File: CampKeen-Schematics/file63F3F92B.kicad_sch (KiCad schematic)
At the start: 36 parts, among them Q42 2N7000, Q43 2N7000, Q44 IRF9Z34NPBF, Q45 IRF9Z34NPBF, Q46 2N7000, Q47 IRF9Z34NPBF, Q48 2N7000, Q49 IRF9Z34NPBF, Q50 2N7000, Q51 IRF9Z34NPBF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

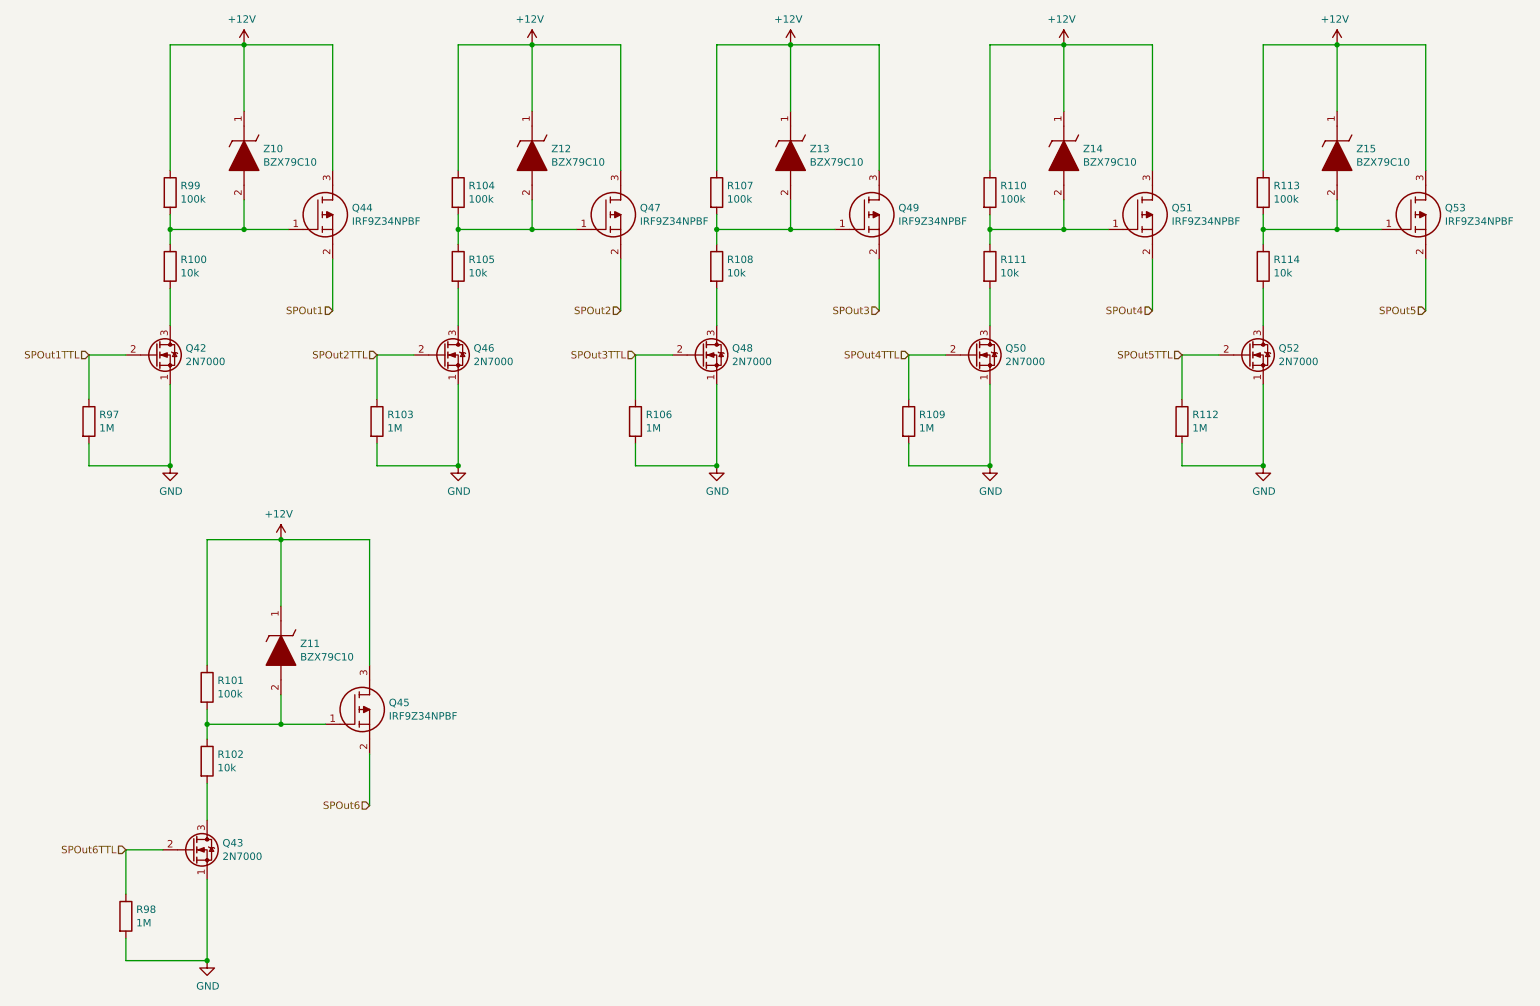
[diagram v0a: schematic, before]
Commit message: alright massive changes. some part switches and some reassignments. mostly it's switching out stuff for SMD so that i have more space.
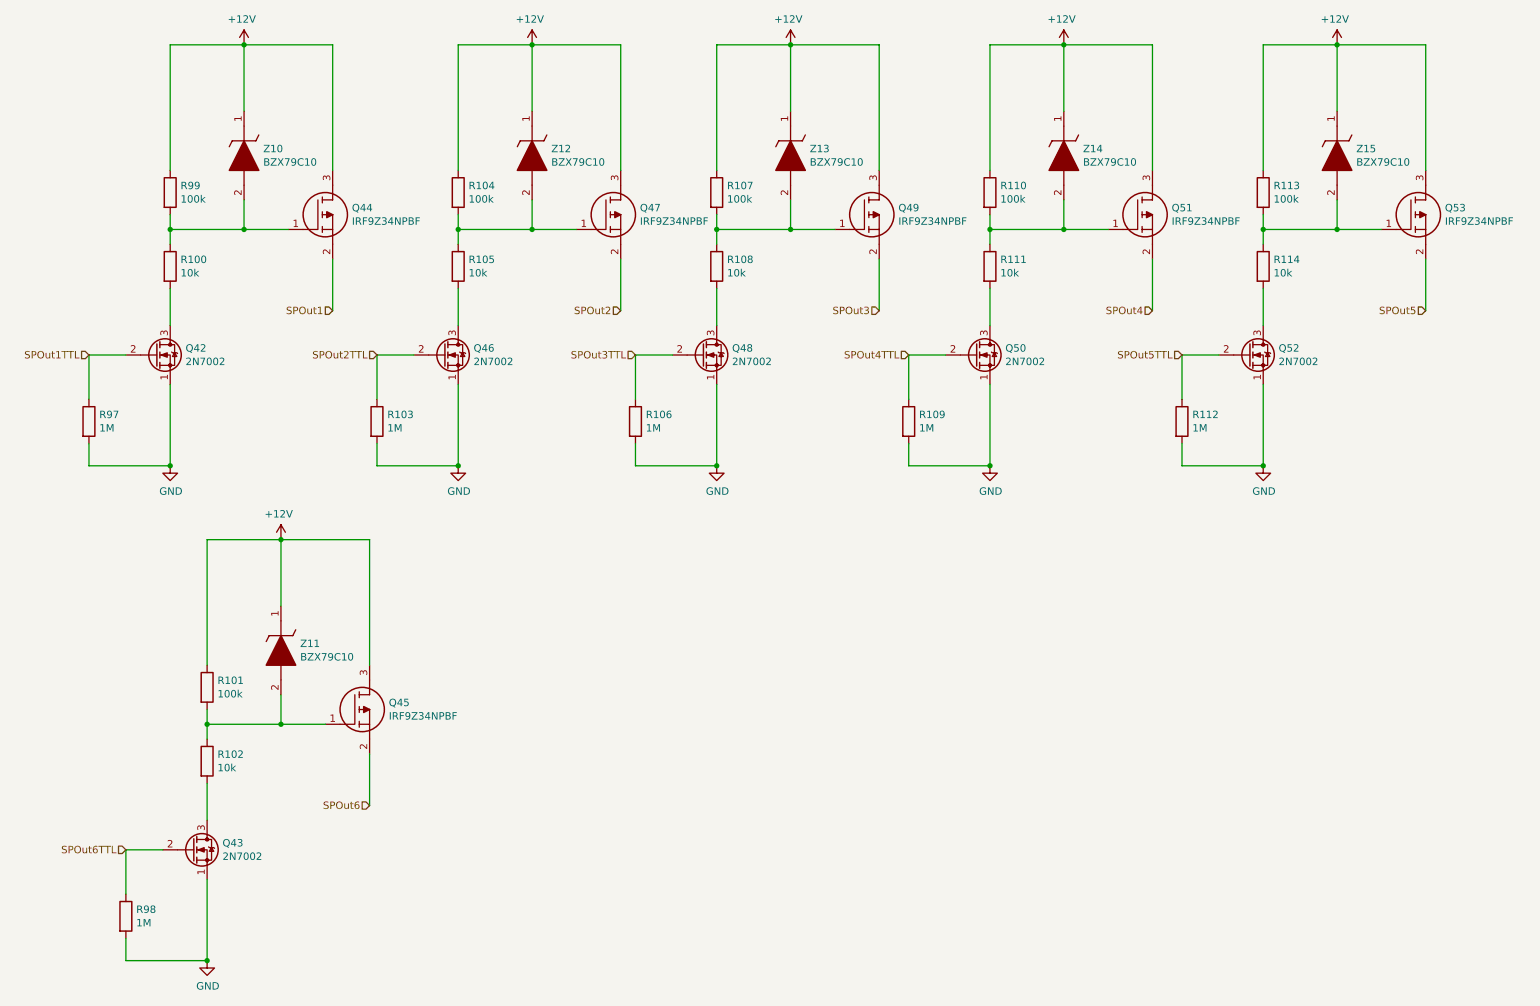
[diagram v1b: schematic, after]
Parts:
- Q42, Q43, Q46, Q48, Q50, Q52: value 2N7000 -> 2N7002; footprint Package_TO_SOT_THT:TO-92_Inline -> Package_TO_SOT_SMD:SOT-23
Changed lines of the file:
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@@
       (effects (font (size 1.27 1.27)) (justify left))
     )
-    (property "Value" "2N7000" (id 1) (at 54.7116 163.703 0)
-      (effects (font (size 1.27 1.27)) (justify left))
-    )
-    (property "Footprint" "Package_TO_SOT_THT:TO-92_Inline" (id 2) (at 54.61 164.465 0)
+    (property "Value" "2N7002" (id 1) (at 54.7116 163.703 0)
+      (effects (font (size 1.27 1.27)) (justify left))
+    )
+    (property "Footprint" "Package_TO_SOT_SMD:SOT-23" (id 2) (at 54.61 164.465 0)
       (effects (font (size 1.27 1.27) italic) (justify left) hide)
     )
@@
       (effects (font (size 1.27 1.27)) (justify left))
     )
-    (property "Value" "2N7000" (id 1) (at 97.8916 78.613 0)
-      (effects (font (size 1.27 1.27)) (justify left))
-    )
-    (property "Footprint" "Package_TO_SOT_THT:TO-92_Inline" (id 2) (at 97.79 79.375 0)
+    (property "Value" "2N7002" (id 1) (at 97.8916 78.613 0)
+      (effects (font (size 1.27 1.27)) (justify left))
+    )
+    (property "Footprint" "Package_TO_SOT_SMD:SOT-23" (id 2) (at 97.79 79.375 0)
       (effects (font (size 1.27 1.27) italic) (justify left) hide)
     )
@@
       (effects (font (size 1.27 1.27)) (justify left))
     )
-    (property "Value" "2N7000" (id 1) (at 142.3416 78.613 0)
-      (effects (font (size 1.27 1.27)) (justify left))
-    )
-    (property "Footprint" "Package_TO_SOT_THT:TO-92_Inline" (id 2) (at 142.24 79.375 0)
+    (property "Value" "2N7002" (id 1) (at 142.3416 78.613 0)
+      (effects (font (size 1.27 1.27)) (justify left))
+    )
+    (property "Footprint" "Package_TO_SOT_SMD:SOT-23" (id 2) (at 142.24 79.375 0)
       (effects (font (size 1.27 1.27) italic) (justify left) hide)
     )
@@
       (effects (font (size 1.27 1.27)) (justify left))
     )
-    (property "Value" "2N7000" (id 1) (at 189.3316 78.613 0)
-      (effects (font (size 1.27 1.27)) (justify left))
-    )
-    (property "Footprint" "Package_TO_SOT_THT:TO-92_Inline" (id 2) (at 189.23 79.375 0)
+    (property "Value" "2N7002" (id 1) (at 189.3316 78.613 0)
+      (effects (font (size 1.27 1.27)) (justify left))
+    )
+    (property "Footprint" "Package_TO_SOT_SMD:SOT-23" (id 2) (at 189.23 79.375 0)
       (effects (font (size 1.27 1.27) italic) (justify left) hide)
     )
@@
       (effects (font (size 1.27 1.27)) (justify left))
     )
-    (property "Value" "2N7000" (id 1) (at 48.3616 78.613 0)
-      (effects (font (size 1.27 1.27)) (justify left))
-    )
-    (property "Footprint" "Package_TO_SOT_THT:TO-92_Inline" (id 2) (at 48.26 79.375 0)
+    (property "Value" "2N7002" (id 1) (at 48.3616 78.613 0)
+      (effects (font (size 1.27 1.27)) (justify left))
+    )
+    (property "Footprint" "Package_TO_SOT_SMD:SOT-23" (id 2) (at 48.26 79.375 0)
       (effects (font (size 1.27 1.27) italic) (justify left) hide)
     )
@@
       (effects (font (size 1.27 1.27)) (justify left))
     )
-    (property "Value" "2N7000" (id 1) (at 236.3216 78.613 0)
-      (effects (font (size 1.27 1.27)) (justify left))
-    )
-    (property "Footprint" "Package_TO_SOT_THT:TO-92_Inline" (id 2) (at 236.22 79.375 0)
+    (property "Value" "2N7002" (id 1) (at 236.3216 78.613 0)
+      (effects (font (size 1.27 1.27)) (justify left))
+    )
+    (property "Footprint" "Package_TO_SOT_SMD:SOT-23" (id 2) (at 236.22 79.375 0)
       (effects (font (size 1.27 1.27) italic) (justify left) hide)
     )
